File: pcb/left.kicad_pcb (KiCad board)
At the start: 2 copper layers, 163.5 x 132.8 mm, 66 parts

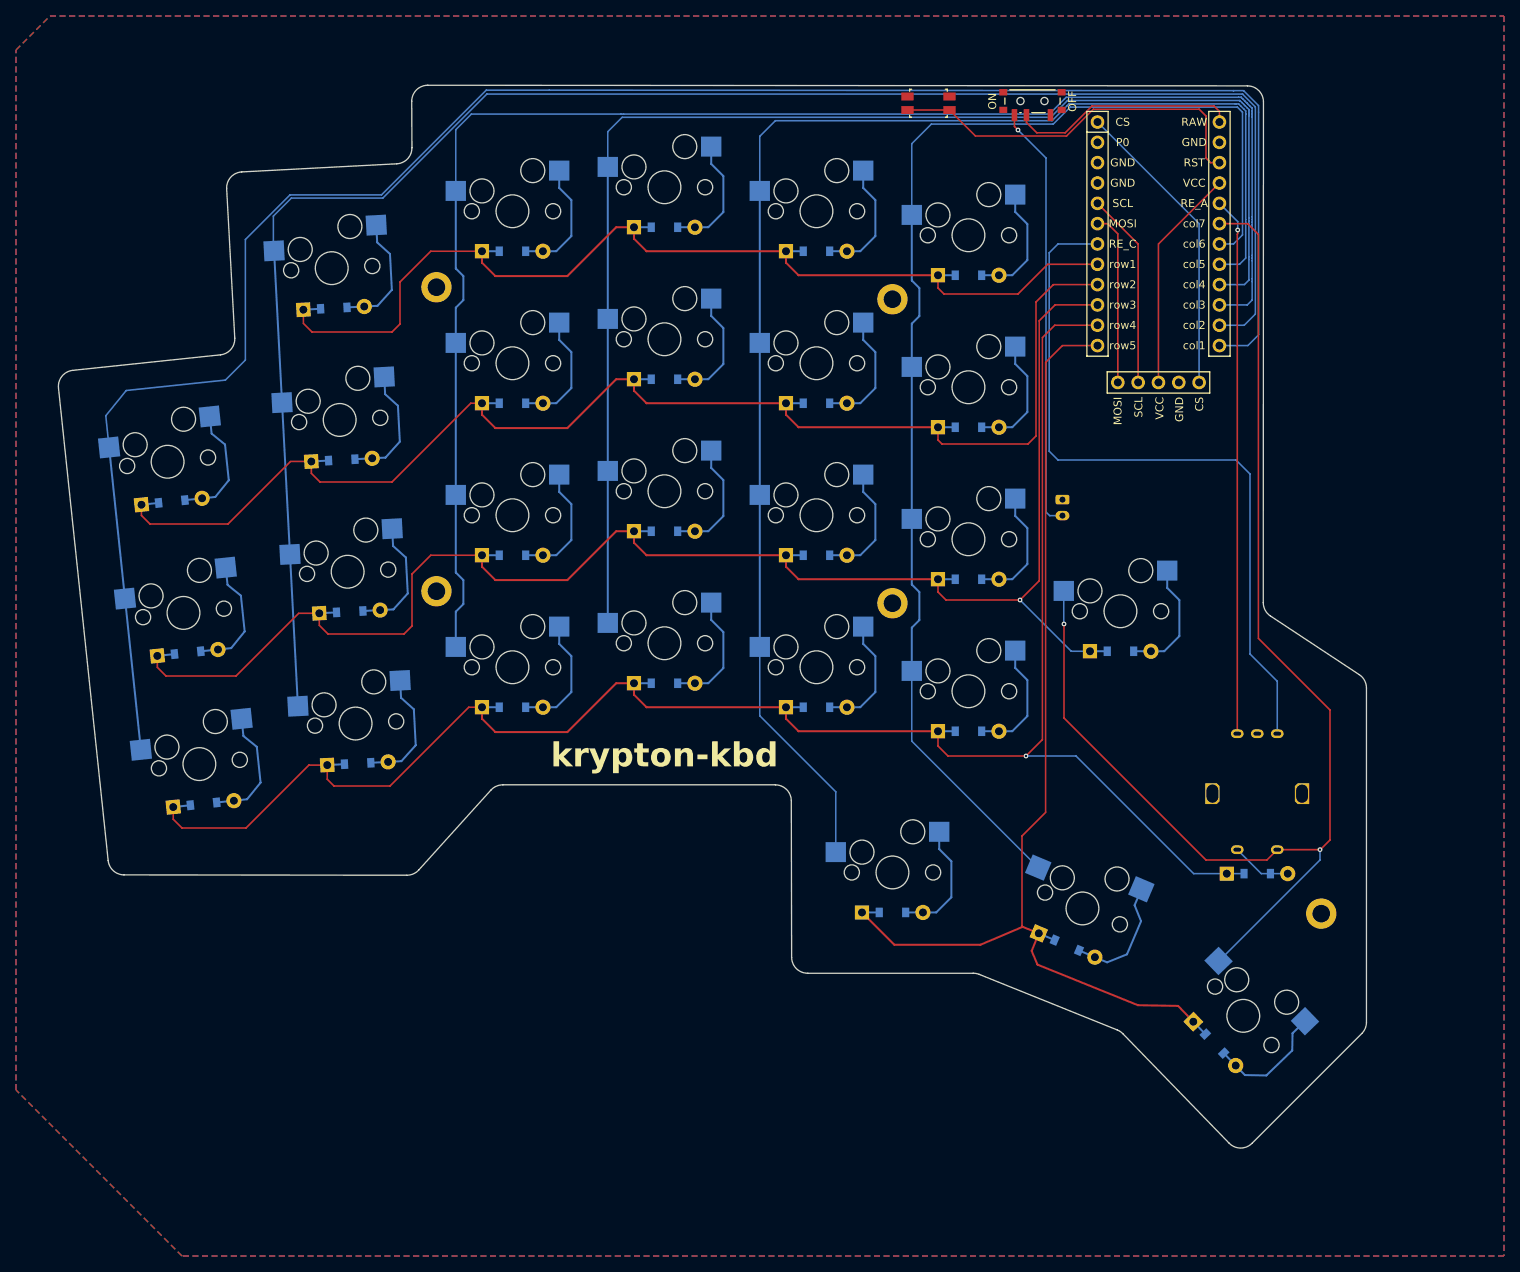
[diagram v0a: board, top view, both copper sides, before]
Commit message: Minor adjustments to pcb routing
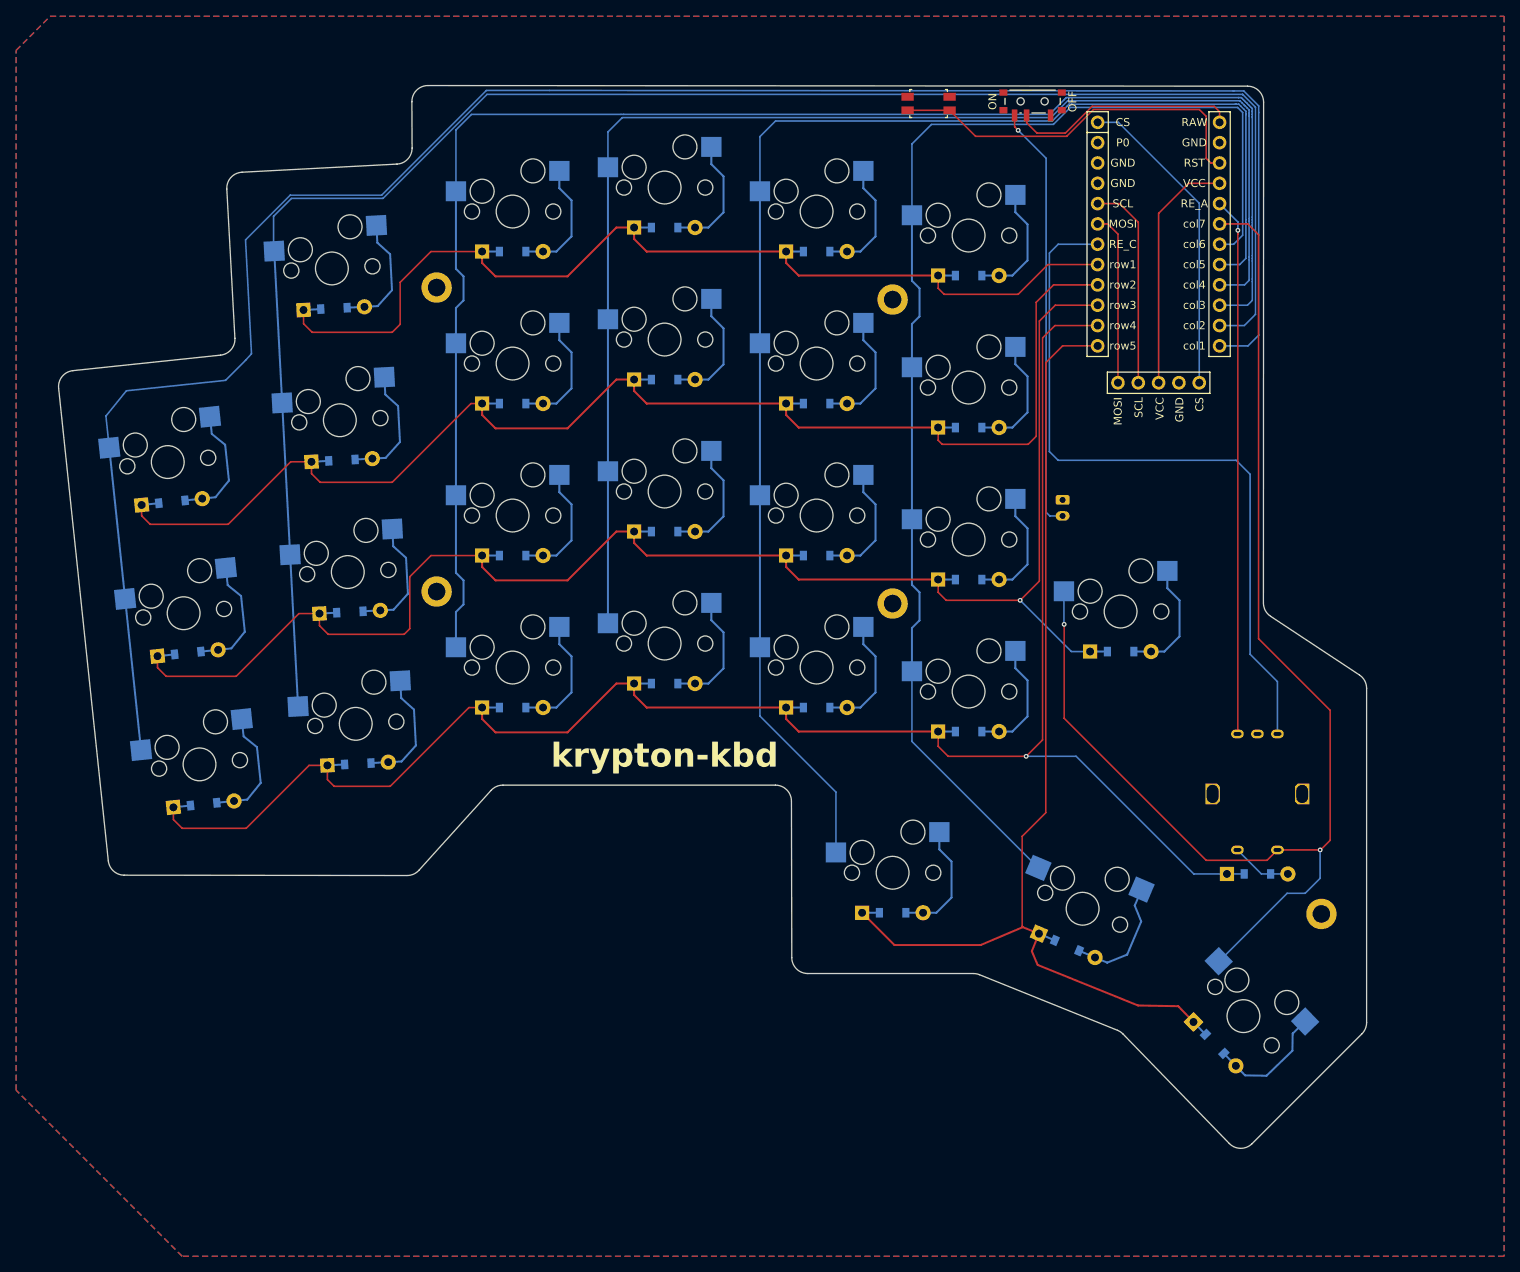
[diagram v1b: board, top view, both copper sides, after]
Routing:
- net VCC: track 28.1 -> 30.3 mm
- net SCL: track 24.5 -> 26.1 mm
- net CS: track 37.8 -> 39.3 mm
- net col7: track 161.6 -> 162.9 mm
